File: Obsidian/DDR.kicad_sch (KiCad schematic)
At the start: 58 parts, among them U2 MT41K512M16HA-125_E / MT41K51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

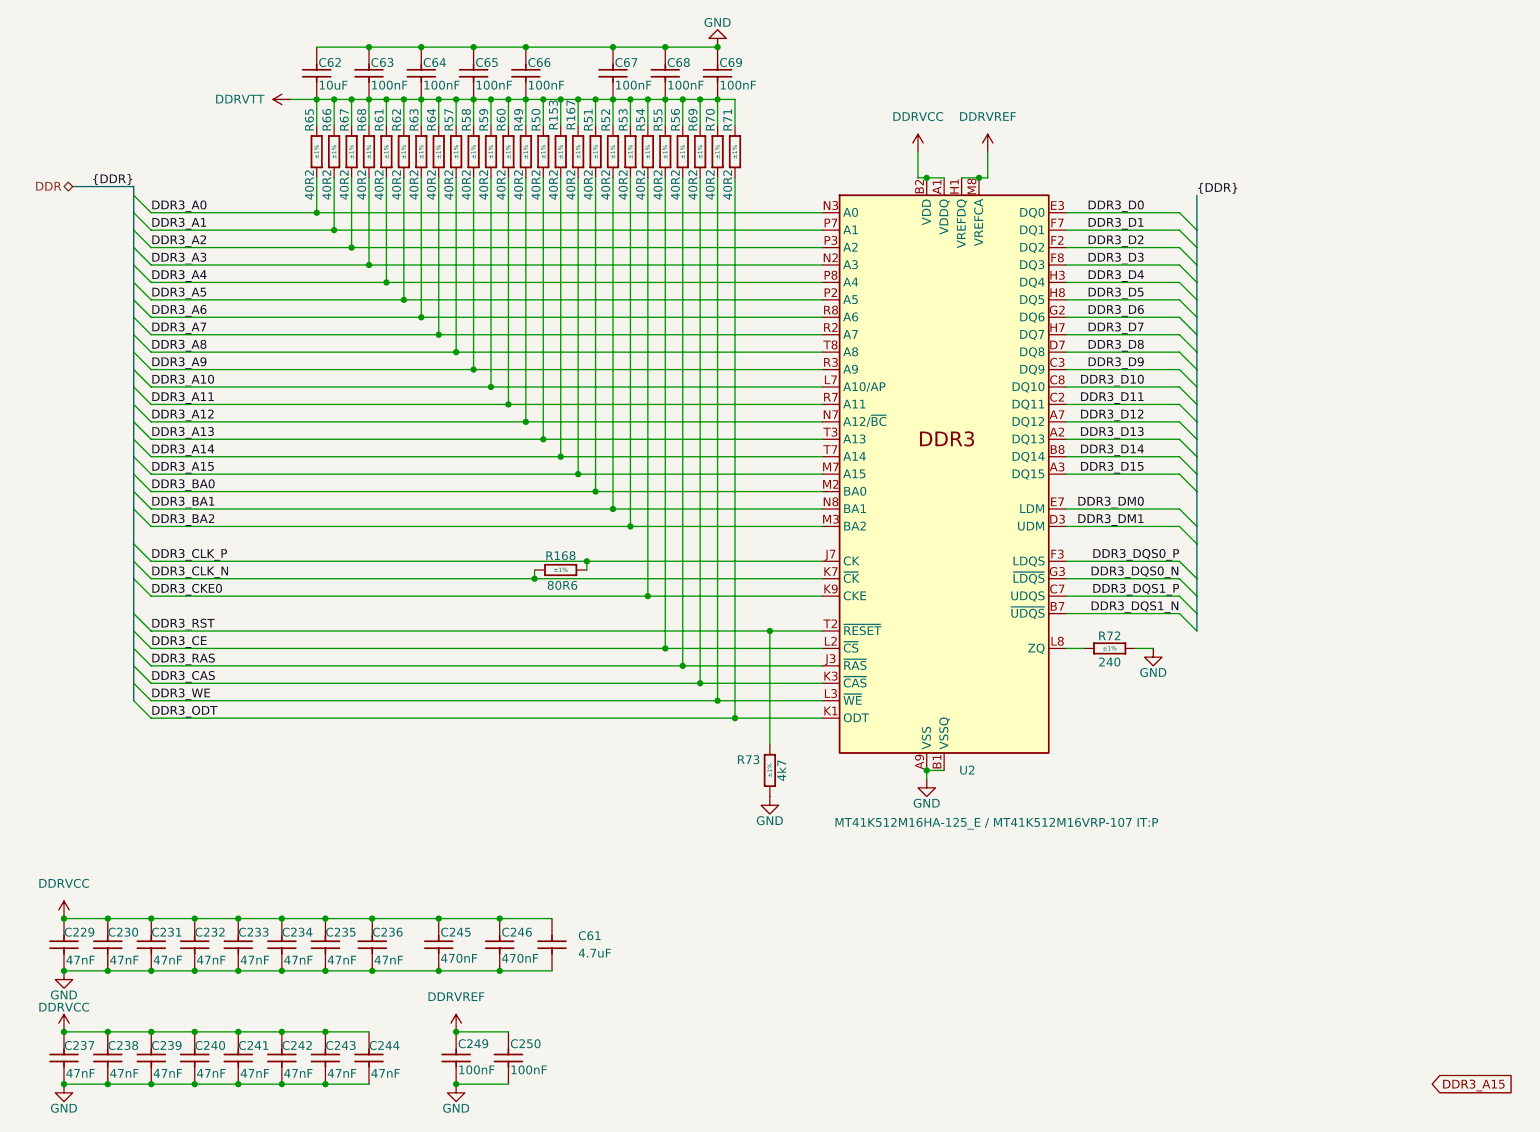
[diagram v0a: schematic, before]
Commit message: Adding symbol library
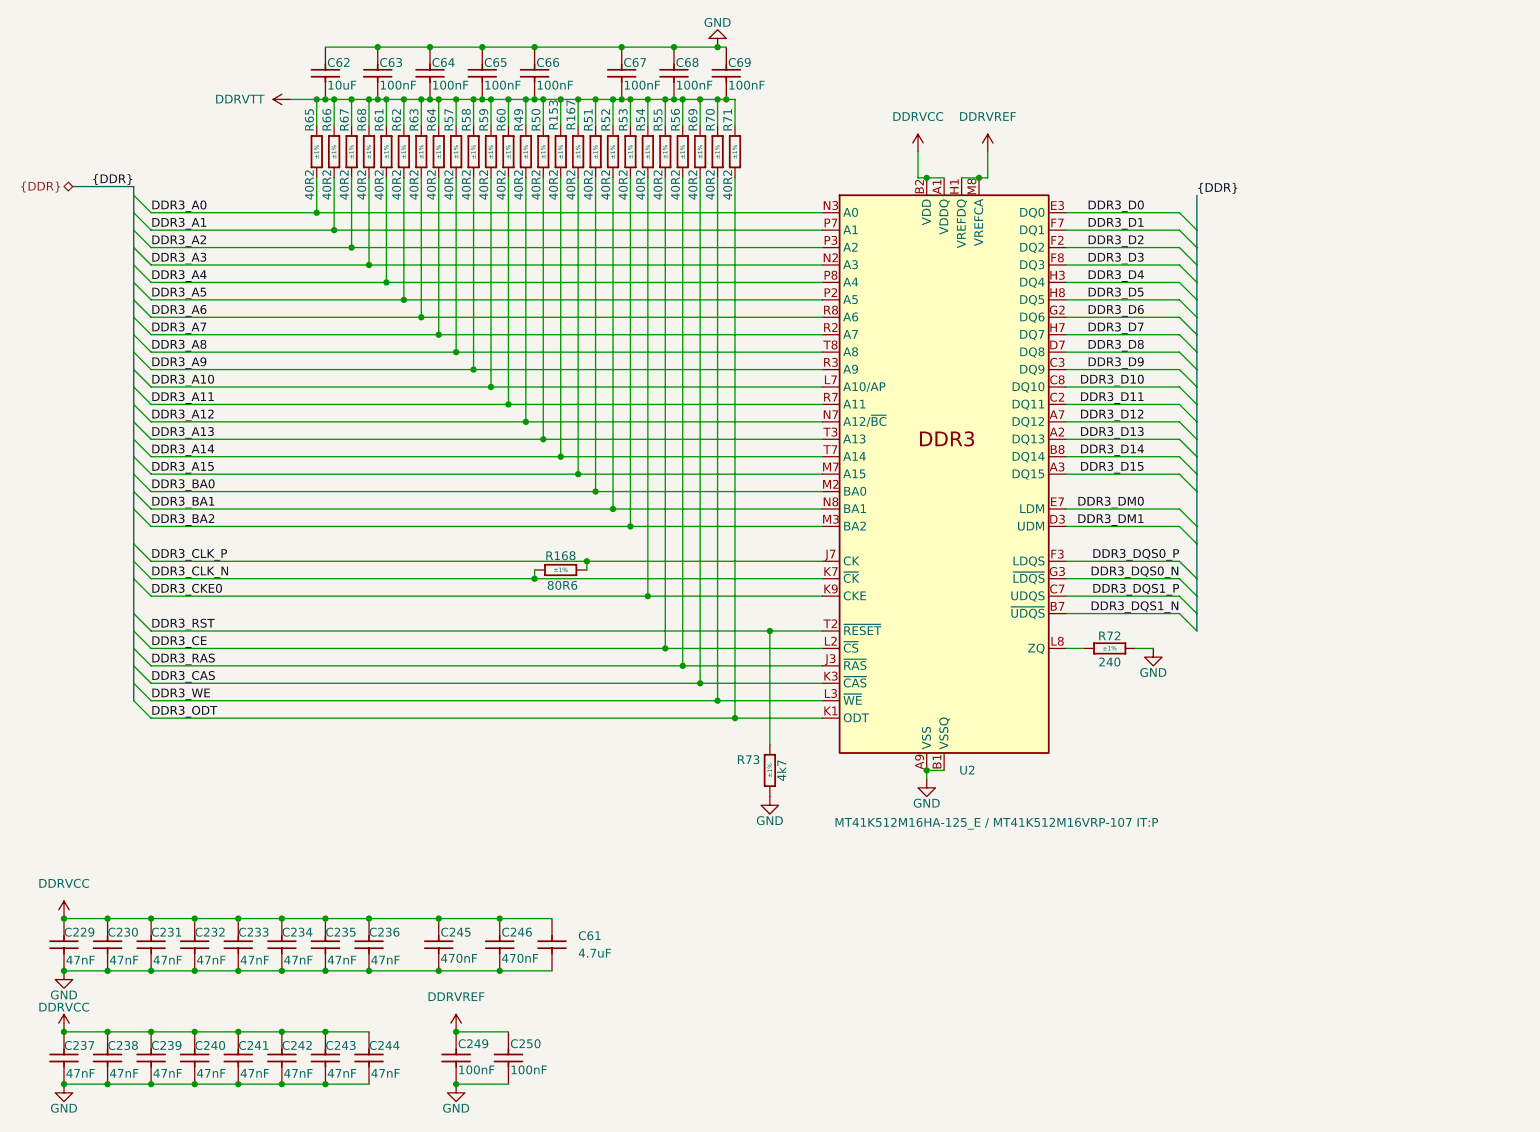
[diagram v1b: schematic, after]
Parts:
- C229, C230, C231, C232, C233, C234, C235, C236, C237, C238, C239, C240, C241, C242, C243, C244: symbol Capacitors SMD:CC0201_47NF_6.3V_10%_X5R -> Library_Symbol:CC0201_47NF_6.3V_10%_X5R
- C245, C246: symbol Capacitors SMD:CC0201_470NF_4V_20%_X5R -> Library_Symbol:CC0201_470NF_4V_20%_X5R
- C249, C250: symbol Capacitors SMD:CC0201_100NF_6.3V_10%_X5R -> Library_Symbol:CC0201_100NF_6.3V_10%_X5R
- C61: symbol Capacitors SMD:CC0402_4.7UF_16V_20%_X5R -> Library_Symbol:CC0402_4.7UF_16V_20%_X5R
- C62: symbol Capacitors SMD:CC0402_10UF_6.3V_20%_X5R -> Library_Symbol:CC0402_10UF_6.3V_20%_X5R
- C63, C64, C65, C66, C67, C68, C69: symbol Capacitors SMD:CC0402_100NF_50V_10%_X7R -> Library_Symbol:CC0402_100NF_50V_10%_X7R
- R153, R167, R49, R50, R51, R52, R53, R54, R55, R56, R57, R58, R59, R60, R61, R62, R63, R64, R65, R66, R67, R68, R69, R70, R71: symbol Resistors SMD:R0402_40R2_1%_0.0625W_100PPM -> Library_Symbol:R0402_40R2_1%_0.0625W_100PPM
- R168: symbol Resistors SMD:R0402_80R6_1%_0.1W_100PPM -> Library_Symbol:R0402_80R6_1%_0.1W_100PPM
- R72: symbol Resistors SMD:R0402_240R_1%_0.0625W_100PPM -> Library_Symbol:R0402_240R_1%_0.0625W_100PPM
- R73: symbol Resistors SMD:R0402_4K7_1%_0.0625W_100PPM -> Library_Symbol:R0402_4K7_1%_0.0625W_100PPM
- U2: symbol Memory_RAM:AS4C256M16D3 -> Library_Symbol:AS4C256M16D3
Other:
- moved on the sheet: C62, C63, C64, C65, C66, C67, C68, C69

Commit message: Correct Schematic errors
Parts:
- C229, C230, C231, C232, C233, C234, C235, C236, C237, C238, C239, C240, C241, C242, C243, C244, C245, C246, C249, C250: footprint Capacitors SMD:CAPC0603X33N -> Footprint:CAPC0603X33N
- C61, C63, C64, C65, C66, C67, C68, C69: footprint Capacitors SMD:CAPC1005X55N -> Footprint:CAPC1005X55N
- C62: footprint Capacitors SMD:CAPC1005X70N -> Footprint:CAPC1005X70N
- R153, R167, R168, R49, R50, R51, R52, R53, R54, R55, R56, R57, R58, R59, R60, R61, R62, R63, R64, R65, R66, R67, R68, R69, R70, R71, R72, R73: footprint Resistors SMD:RESC1005X40N -> Footprint:RESC1005X40N
- U2: footprint Package_BGA:FBGA-96_9x14mm_Layout9x16_P0.8mm -> Footprint:FBGA-96_9x14mm_Layout9x16_P0.8mm
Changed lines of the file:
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@@
 			)
 		)
-		(property "Footprint" "Resistors SMD:RESC1005X40N"
+		(property "Footprint" "Footprint:RESC1005X40N"
 			(at 118.618 52.07 0)
 			(effects
@@
 			)
 		)
-		(property "Footprint" "Resistors SMD:RESC1005X40N"
+		(property "Footprint" "Footprint:RESC1005X40N"
 			(at 133.858 52.07 0)
 			(effects
@@
 			)
 		)
-		(property "Footprint" "Capacitors SMD:CAPC0603X33N"
+		(property "Footprint" "Footprint:CAPC0603X33N"
 			(at 70.358 184.15 0)
 			(effects
@@
 			)
 		)
-		(property "Footprint" "Capacitors SMD:CAPC0603X33N"
+		(property "Footprint" "Footprint:CAPC0603X33N"
 			(at 99.568 167.64 0)
 			(effects
@@
 			)
 		)
-		(property "Footprint" "Resistors SMD:RESC1005X40N"
+		(property "Footprint" "Footprint:RESC1005X40N"
 			(at 105.918 52.07 0)
 			(effects
@@
 			)
 		)
-		(property "Footprint" "Resistors SMD:RESC1005X40N"
+		(property "Footprint" "Footprint:RESC1005X40N"
 			(at 95.758 52.07 0)
 			(effects
@@
 			)
 		)
-		(property "Footprint" "Resistors SMD:RESC1005X40N"
+		(property "Footprint" "Footprint:RESC1005X40N"
 			(at 93.218 52.07 0)
 			(effects
@@
 			)
 		)
-		(property "Footprint" "Capacitors SMD:CAPC0603X33N"
+		(property "Footprint" "Footprint:CAPC0603X33N"
 			(at 108.458 167.64 0)
 			(effects
@@
 			)
 		)
-		(property "Footprint" "Resistors SMD:RESC1005X40N"
+		(property "Footprint" "Footprint:RESC1005X40N"
 			(at 108.458 52.07 0)
 			(effects
@@
 			)
 		)
-		(property "Footprint" "Capacitors SMD:CAPC0603X33N"
+		(property "Footprint" "Footprint:CAPC0603X33N"
 			(at 89.408 184.15 0)
 			(effects
@@
 			)
 		)
-		(property "Footprint" "Capacitors SMD:CAPC0603X33N"
+		(property "Footprint" "Footprint:CAPC0603X33N"
 			(at 51.308 167.64 0)
 			(effects
@@
 			)
 		)
-		(property "Footprint" "Capacitors SMD:CAPC0603X33N"
+		(property "Footprint" "Footprint:CAPC0603X33N"
 			(at 83.058 167.64 0)
 			(effects
@@
 			)
 		)
-		(property "Footprint" "Capacitors SMD:CAPC1005X55N"
+		(property "Footprint" "Footprint:CAPC1005X55N"
 			(at 116.078 167.64 0)
 			(effects
@@
 			)
 		)
-		(property "Footprint" "Capacitors SMD:CAPC0603X33N"
+		(property "Footprint" "Footprint:CAPC0603X33N"
 			(at 70.358 167.64 0)
 			(effects
@@
 			)
 		)
-		(property "Footprint" "Resistors SMD:RESC1005X40N"
+		(property "Footprint" "Footprint:RESC1005X40N"
 			(at 80.518 52.07 0)
 			(effects
@@
 			)
 		)
-		(property "Footprint" "Capacitors SMD:CAPC0603X33N"
+		(property "Footprint" "Footprint:CAPC0603X33N"
 			(at 76.708 167.64 0)
 			(effects
@@
 			)
 		)
-		(property "Footprint" "Capacitors SMD:CAPC1005X55N"
+		(property "Footprint" "Footprint:CAPC1005X55N"
 			(at 141.478 40.64 0)
 			(effects
@@
 			)
 		)
-		(property "Footprint" "Resistors SMD:RESC1005X40N"
+		(property "Footprint" "Footprint:RESC1005X40N"
 			(at 131.318 52.07 0)
 			(effects
@@
 			)
 		)
-		(property "Footprint" "Resistors SMD:RESC1005X40N"
+		(property "Footprint" "Footprint:RESC1005X40N"
 			(at 103.378 52.07 0)
 			(effects
@@
 			)
 		)
-		(property "Footprint" "Capacitors SMD:CAPC0603X33N"
+		(property "Footprint" "Footprint:CAPC0603X33N"
 			(at 44.958 167.64 0)
 			(effects
@@
 			)
 		)
-		(property "Footprint" "Capacitors SMD:CAPC1005X55N"
+		(property "Footprint" "Footprint:CAPC1005X55N"
 			(at 113.538 40.64 0)
 			(effects
@@
 			)
 		)
-		(property "Footprint" "Resistors SMD:RESC1005X40N"
+		(property "Footprint" "Footprint:RESC1005X40N"
 			(at 126.238 52.07 0)
 			(effects
@@
 			)
 		)
-		(property "Footprint" "Resistors SMD:RESC1005X40N"
+		(property "Footprint" "Footprint:RESC1005X40N"
 			(at 138.938 52.07 0)
 			(effects
@@
 			)
 		)
-		(property "Footprint" "Capacitors SMD:CAPC1005X55N"
+		(property "Footprint" "Footprint:CAPC1005X55N"
 			(at 98.298 40.64 0)
 			(effects
@@
 			)
 		)
-		(property "Footprint" "Resistors SMD:RESC1005X40N"
+		(property "Footprint" "Footprint:RESC1005X40N"
 			(at 146.558 142.24 0)
 			(effects
@@
 			)
 		)
-		(property "Footprint" "Resistors SMD:RESC1005X40N"
+		(property "Footprint" "Footprint:RESC1005X40N"
 			(at 128.778 52.07 0)
 			(effects
@@
 			)
 		)
-		(property "Footprint" "Resistors SMD:RESC1005X40N"
+		(property "Footprint" "Footprint:RESC1005X40N"
 			(at 105.41 116.078 0)
 			(effects
@@
 			)
 		)
-		(property "Footprint" "Capacitors SMD:CAPC1005X70N"
+		(property "Footprint" "Footprint:CAPC1005X70N"
 			(at 83.058 40.64 0)
 			(effects
@@
 			)
 		)
-		(property "Footprint" "Resistors SMD:RESC1005X40N"
+		(property "Footprint" "Footprint:RESC1005X40N"
 			(at 185.42 127.508 0)
 			(effects
@@
 			)
 		)
-		(property "Footprint" "Capacitors SMD:CAPC0603X33N"
+		(property "Footprint" "Footprint:CAPC0603X33N"
 			(at 51.308 184.15 0)
 			(effects
@@
 			)
 		)
-		(property "Footprint" "Resistors SMD:RESC1005X40N"
+		(property "Footprint" "Footprint:RESC1005X40N"
 			(at 123.698 52.07 0)
 			(effects
@@
 			)
 		)
-		(property "Footprint" "Resistors SMD:RESC1005X40N"
+		(property "Footprint" "Footprint:RESC1005X40N"
 			(at 90.678 52.07 0)
 			(effects
@@
 			)
 		)
-		(property "Footprint" "Resistors SMD:RESC1005X40N"
+		(property "Footprint" "Footprint:RESC1005X40N"
 			(at 88.138 52.07 0)
 			(effects
@@
 			)
 		)
-		(property "Footprint" "Capacitors SMD:CAPC0603X33N"
+		(property "Footprint" "Footprint:CAPC0603X33N"
 			(at 44.958 184.15 0)
 			(effects
@@
 			)
 		)
-		(property "Footprint" "Capacitors SMD:CAPC0603X33N"
+		(property "Footprint" "Footprint:CAPC0603X33N"
 			(at 83.058 184.15 0)
 			(effects
@@
 			)
 		)
-		(property "Footprint" "Capacitors SMD:CAPC0603X33N"
+		(property "Footprint" "Footprint:CAPC0603X33N"
 			(at 57.658 184.15 0)
 			(effects
@@
 			)
 		)
-		(property "Footprint" "Resistors SMD:RESC1005X40N"
+		(property "Footprint" "Footprint:RESC1005X40N"
 			(at 100.838 52.07 0)
 			(effects
@@
 			)
 		)
-		(property "Footprint" "Capacitors SMD:CAPC0603X33N"
+		(property "Footprint" "Footprint:CAPC0603X33N"
 			(at 57.658 167.64 0)
 			(effects
@@
 			)
 		)
-		(property "Footprint" "Package_BGA:FBGA-96_9x14mm_Layout9x16_P0.8mm"
+		(property "Footprint" "Footprint:FBGA-96_9x14mm_Layout9x16_P0.8mm"
 			(at 163.83 49.53 0)
 			(effects
@@
 			)
 		)
-		(property "Footprint" "Resistors SMD:RESC1005X40N"
+		(property "Footprint" "Footprint:RESC1005X40N"
 			(at 85.598 52.07 0)
 			(effects
@@
 			)
 		)
-		(property "Footprint" "Capacitors SMD:CAPC0603X33N"
+		(property "Footprint" "Footprint:CAPC0603X33N"
 			(at 89.408 167.64 0)
 			(effects
@@
 			)
 		)
-		(property "Footprint" "Capacitors SMD:CAPC0603X33N"
+		(property "Footprint" "Footprint:CAPC0603X33N"
 			(at 64.008 167.64 0)
 			(effects
@@
 			)
 		)
-		(property "Footprint" "Resistors SMD:RESC1005X40N"
+		(property "Footprint" "Footprint:RESC1005X40N"
 			(at 116.078 52.07 0)
 			(effects
@@
 			)
 		)
-		(property "Footprint" "Capacitors SMD:CAPC0603X33N"
+		(property "Footprint" "Footprint:CAPC0603X33N"
 			(at 64.008 184.15 0)
 			(effects
@@
 			)
 		)
-		(property "Footprint" "Resistors SMD:RESC1005X40N"
+		(property "Footprint" "Footprint:RESC1005X40N"
 			(at 110.998 52.07 0)
 			(effects
@@
 			)
 		)
-		(property "Footprint" "Capacitors SMD:CAPC0603X33N"
+		(property "Footprint" "Footprint:CAPC0603X33N"
 			(at 76.708 184.15 0)
 			(effects
@@
 			)
 		)
-		(property "Footprint" "Resistors SMD:RESC1005X40N"
+		(property "Footprint" "Footprint:RESC1005X40N"
 			(at 83.058 52.07 0)
 			(effects
@@
 			)
 		)
-		(property "Footprint" "Capacitors SMD:CAPC1005X55N"
+		(property "Footprint" "Footprint:CAPC1005X55N"
 			(at 105.918 40.64 0)
 			(effects
@@
 			)
 		)
-		(property "Footprint" "Capacitors SMD:CAPC1005X55N"
+		(property "Footprint" "Footprint:CAPC1005X55N"
 			(at 90.678 40.64 0)
 			(effects
@@
 			)
 		)
-		(property "Footprint" "Capacitors SMD:CAPC0603X33N"
+		(property "Footprint" "Footprint:CAPC0603X33N"
 			(at 102.108 184.15 0)
 			(effects
@@
 			)
 		)
-		(property "Footprint" "Resistors SMD:RESC1005X40N"
+		(property "Footprint" "Footprint:RESC1005X40N"
 			(at 113.538 52.07 0)
 			(effects
@@
 			)
 		)
-		(property "Footprint" "Capacitors SMD:CAPC0603X33N"
+		(property "Footprint" "Footprint:CAPC0603X33N"
 			(at 109.728 184.15 0)
 			(effects
@@
 			)
 		)
-		(property "Footprint" "Capacitors SMD:CAPC1005X55N"
+		(property "Footprint" "Footprint:CAPC1005X55N"
 			(at 133.858 40.64 0)
 			(effects
@@
 			)
 		)
-		(property "Footprint" "Resistors SMD:RESC1005X40N"
+		(property "Footprint" "Footprint:RESC1005X40N"
 			(at 141.478 52.07 0)
 			(effects
@@
 			)
 		)
-		(property "Footprint" "Resistors SMD:RESC1005X40N"
+		(property "Footprint" "Footprint:RESC1005X40N"
 			(at 136.398 52.07 0)
 			(effects
@@
 			)
 		)
-		(property "Footprint" "Capacitors SMD:CAPC1005X55N"
+		(property "Footprint" "Footprint:CAPC1005X55N"
 			(at 126.238 40.64 0)
 			(effects
@@
 			)
 		)
-		(property "Footprint" "Resistors SMD:RESC1005X40N"
+		(property "Footprint" "Footprint:RESC1005X40N"
 			(at 121.158 52.07 0)
 			(effects
@@
 			)
 		)
-		(property "Footprint" "Resistors SMD:RESC1005X40N"
+		(property "Footprint" "Footprint:RESC1005X40N"
 			(at 98.298 52.07 0)
 			(effects

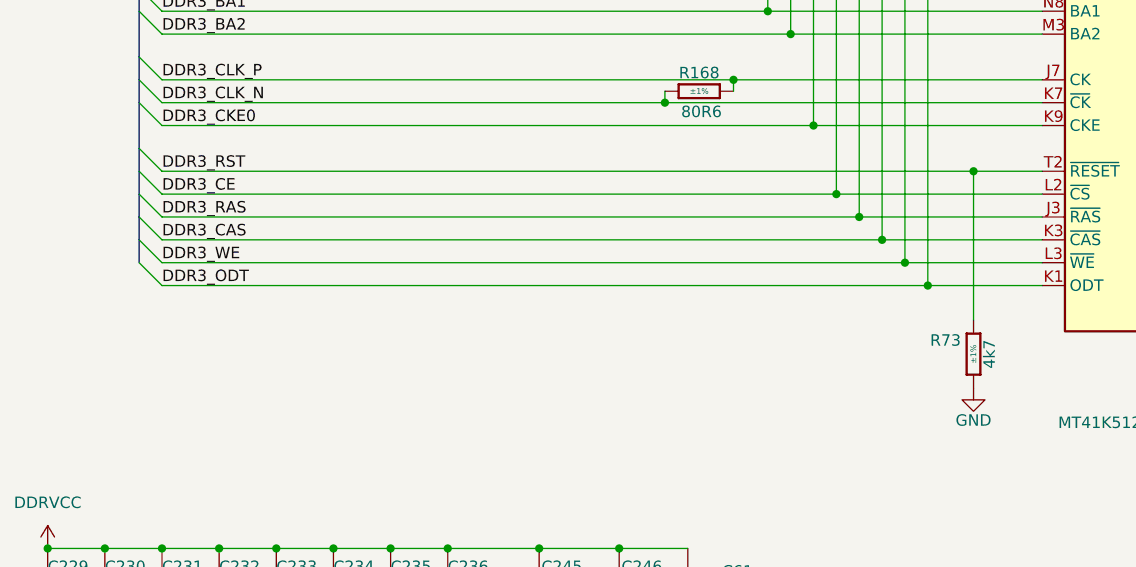
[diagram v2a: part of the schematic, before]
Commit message: adding lcsc reference for PMOD
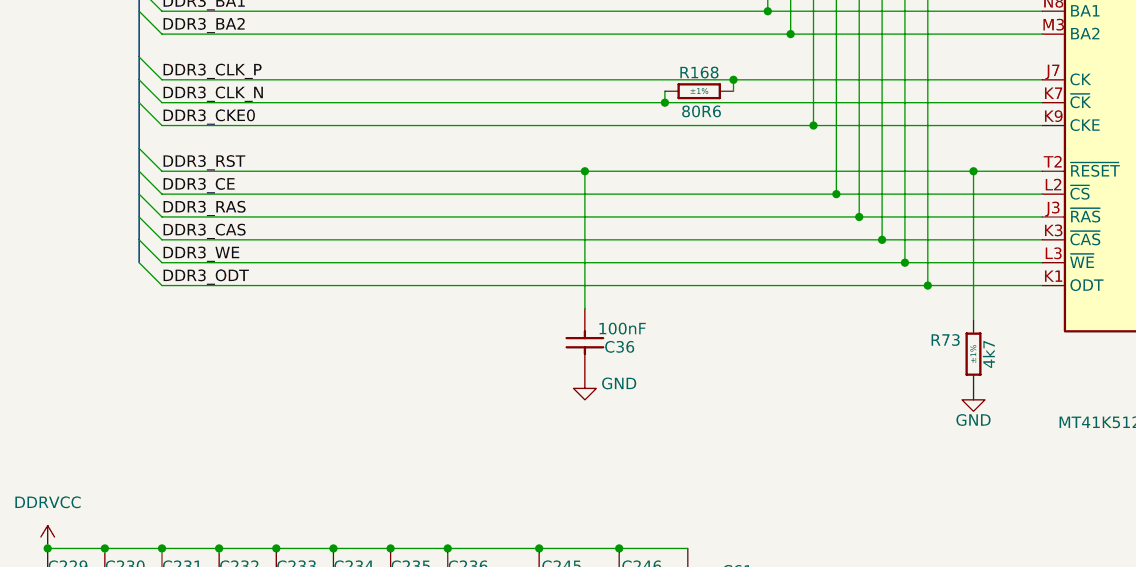
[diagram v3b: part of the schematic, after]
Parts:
- added C36: CC0402_100NF_50V_10%_X7R, Capacitor_SMD:C_0402_1005Metric, symbol Library_Symbol:CC0402_100NF_50V_10%_X7R
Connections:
- net DDR3_RST: now also C36.1
- net GND: now also C36.2

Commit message: update LCSC reference, and OFFSET rotation for JLCPCB
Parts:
- C36: footprint Capacitor_SMD:C_0402_1005Metric -> Footprint:CAPC1005X55N
- R72: LCSC C25094 -> C114755
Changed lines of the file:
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@@
 			)
 		)
-		(property "LCSC" "C25094"
+		(property "LCSC" "C114755"
 			(at 185.42 120.65 0)
 			(effects
@@
 			)
 		)
-		(property "Footprint" "Capacitor_SMD:C_0402_1005Metric"
+		(property "Footprint" "Footprint:CAPC1005X55N"
 			(at 88.392 133.35 0)
 			(effects
